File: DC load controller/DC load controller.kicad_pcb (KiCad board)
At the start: 2 copper layers, 50 x 25 mm, 24 parts, among them J1 Ctrl In, J2 Batt in, J3 Ctrl Out, J4 Pwr in, M1 3mm, M2 3mm, M3 3mm, U1 LM324

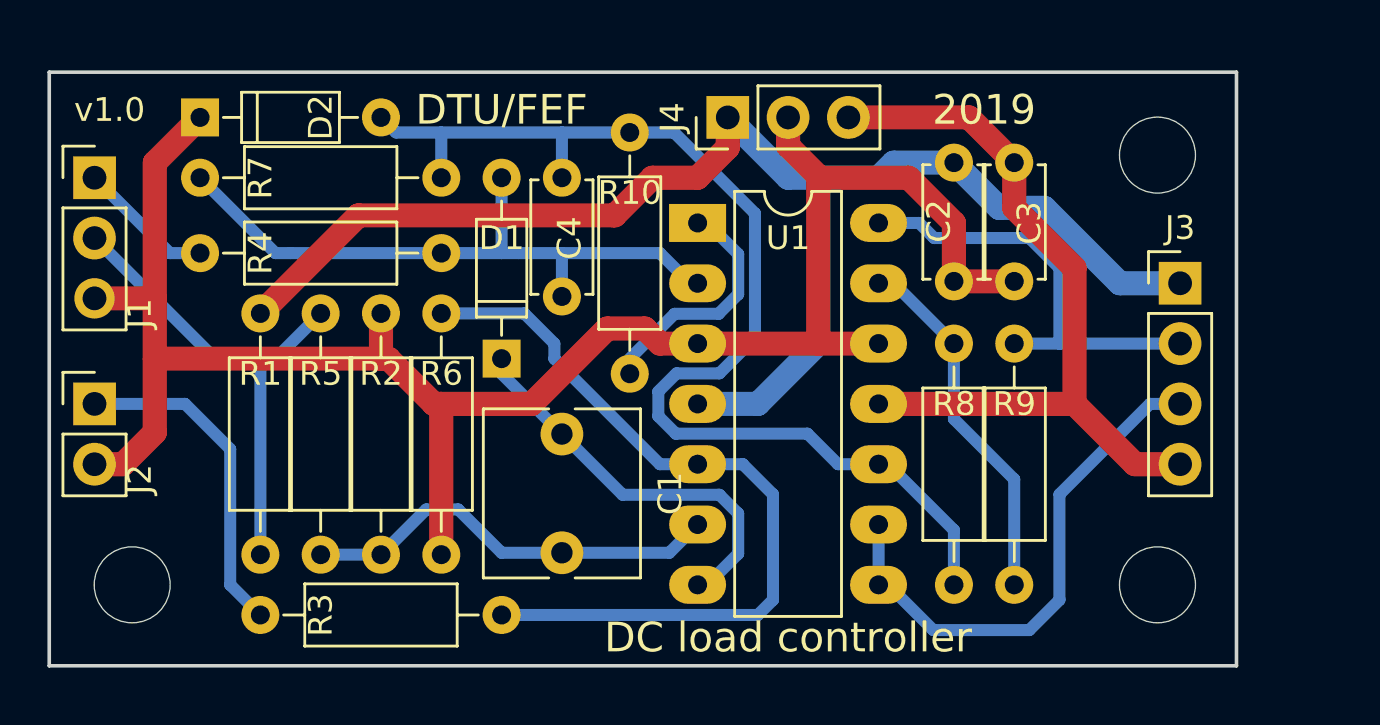
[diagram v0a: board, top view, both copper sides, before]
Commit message: Added output driver transistors
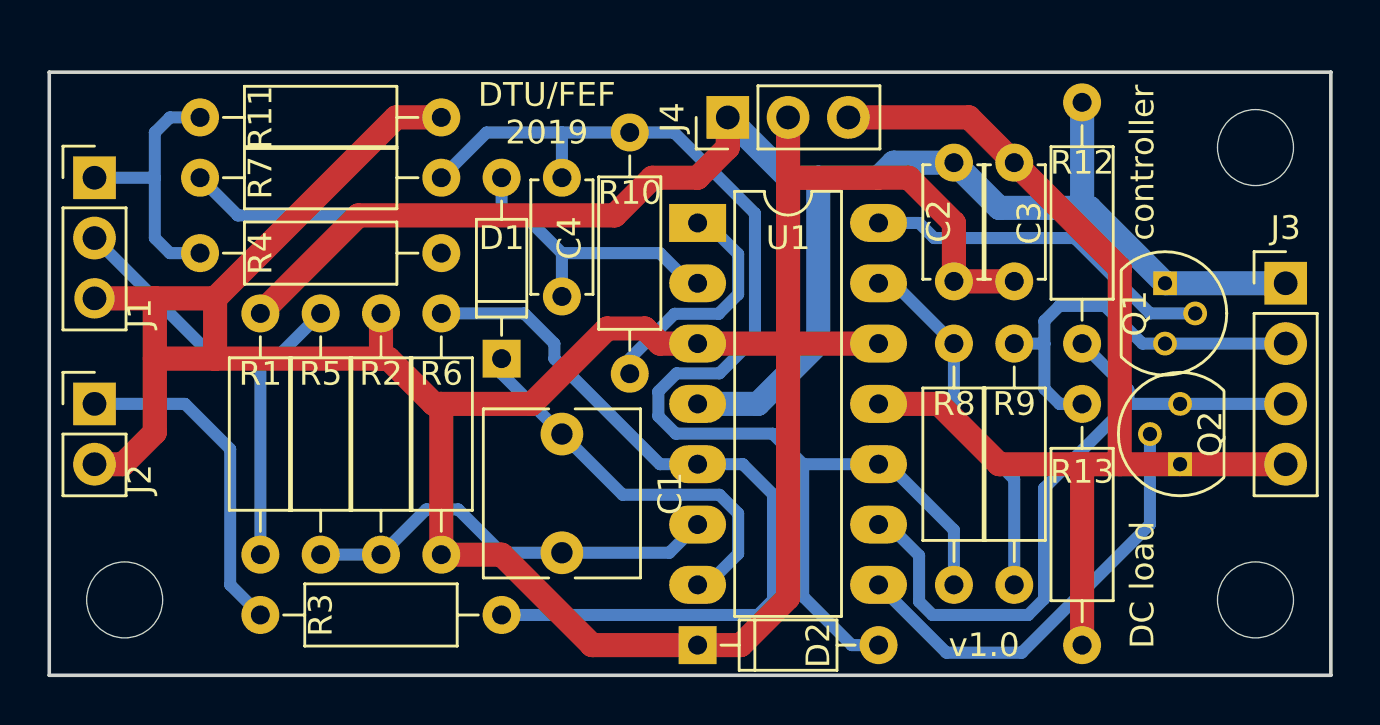
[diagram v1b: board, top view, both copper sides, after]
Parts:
- added Q1: BC547, TO_SOT_Packages_THT:TO-92_Molded_Narrow, F.Cu at (148.6, 72.4)
- added Q2: BC557, TO_SOT_Packages_THT:TO-92_Molded_Narrow, F.Cu at (149.2, 80.0)
- added R11: 1k, Resistors_THT:R_Axial_DIN0207_L6.3mm_D2.5mm_P10.16mm_Horizontal, F.Cu at (108.0, 65.4)
- added R12: 10k, Resistors_THT:R_Axial_DIN0207_L6.3mm_D2.5mm_P10.16mm_Horizontal, F.Cu at (145.1, 64.8)
- added R13: 10k, Resistors_THT:R_Axial_DIN0207_L6.3mm_D2.5mm_P10.16mm_Horizontal, F.Cu at (145.1, 77.5)
- moved D2 30.5 mm to (128.9, 87.6)
- moved J3 4.44 mm to (153.7, 72.4)
- moved M2 4.18 mm to (152.4, 85.7)
- moved M3 4.14 mm to (152.4, 66.7)
- moved M1 0.71 mm to (104.8, 85.7)
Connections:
- R4 pad 1: Net-(C4-Pad1) -> Net-(R4-Pad1)
- U1 pad 14: Net-(J3-Pad2) -> Net-(Q1-Pad2)
- U1 pad 8: Net-(J3-Pad3) -> Net-(Q2-Pad2)
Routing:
- net GND: track 83.2 -> 121.0 mm
- net Net-(Q2-Pad2): track 0.00 -> 19.1 mm
- net VSS: track 32.7 -> 48.3 mm
- net Net-(Q1-Pad2): track 0.00 -> 15.4 mm
- net VDD: track 59.4 -> 68.3 mm
- net Net-(J3-Pad3): track 23.0 -> 30.0 mm
- net Net-(C4-Pad2): track 49.3 -> 54.9 mm
- net Net-(J1-Pad1): track 5.76 -> 11.3 mm
- net Net-(J3-Pad2): track 19.4 -> 17.1 mm
- net Net-(C4-Pad1): track 28.2 -> 26.6 mm
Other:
- board size 50 x 25 mm -> 54 x 25.4 mm
- board text added: "DC load"
- board text added: "controller"
- board text removed: "DC load controller"
